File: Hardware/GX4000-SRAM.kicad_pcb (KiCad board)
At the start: 2 copper layers, 7 parts, among them U1 IS62C1024AL-35QLI, U2 74HCT573, U3 74LVC1G32, U4 TMS4464, U5 TMS4464

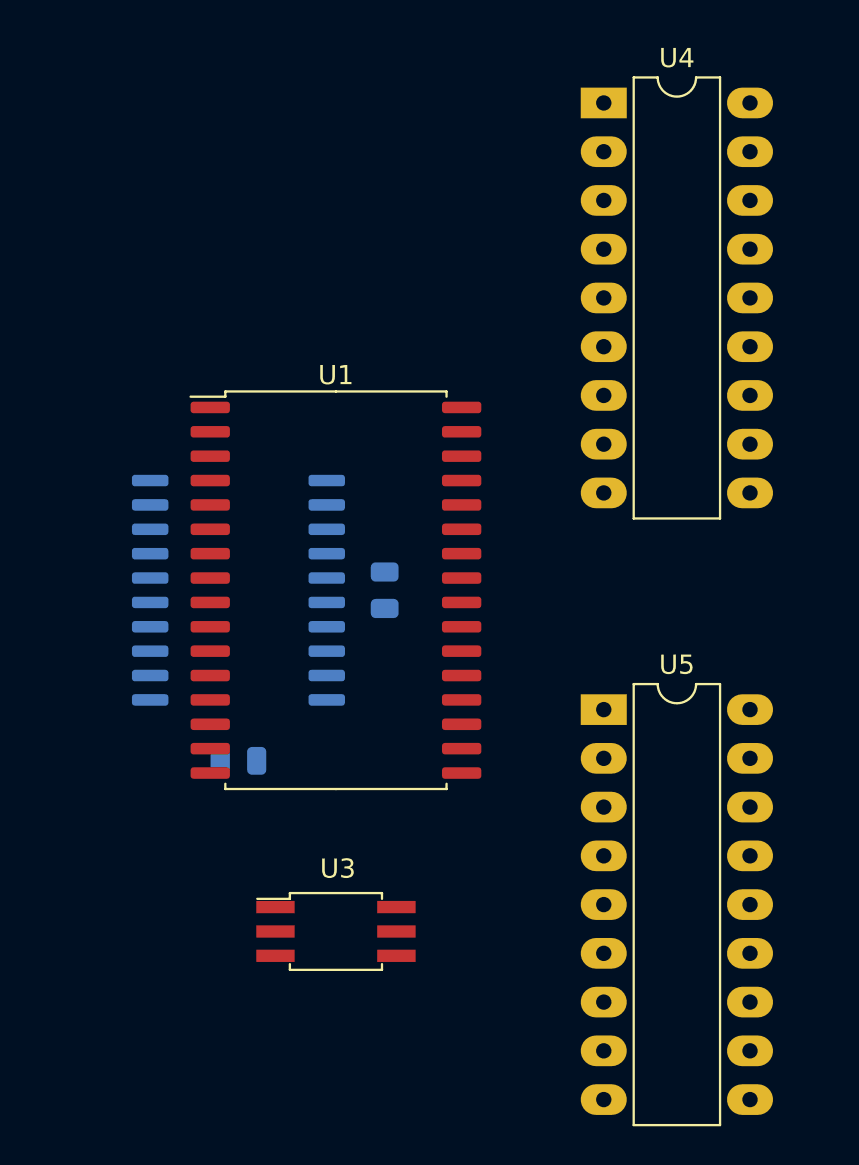
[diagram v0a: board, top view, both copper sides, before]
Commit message: Fixes the expacement between U10 and U11
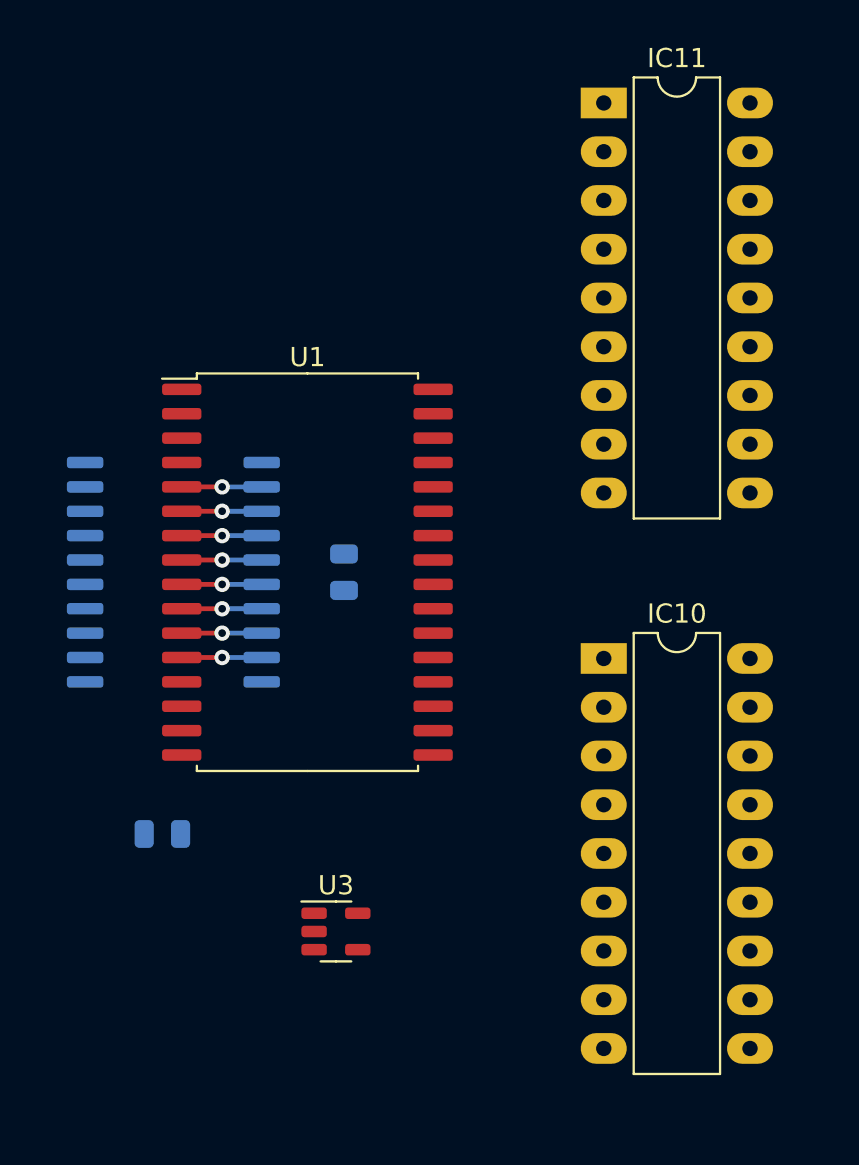
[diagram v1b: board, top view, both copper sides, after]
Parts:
- U3: footprint Package_SO:SO-6_4.4x3.6mm_P1.27mm -> Package_TO_SOT_SMD:SOT-23-5
- moved C1 5.50 mm to (128.1, 104.1)
- moved U2 3.52 mm to (128.7, 90.5)
- moved IC10 2.66 mm to (151.1, 95.0)
- moved C2 2.32 mm to (137.6, 90.5)
- moved U1 1.76 mm to (135.7, 90.5)
- renumbered U5 to IC10, U4 to IC11
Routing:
- net /A7: track 0.00 -> 4.16 mm, vias 0 -> 1
- net /A6: track 0.00 -> 4.16 mm, vias 0 -> 1
- net /A5: track 0.00 -> 4.16 mm, vias 0 -> 1
- net /A4: track 0.00 -> 4.16 mm, vias 0 -> 1
- net /A3: track 0.00 -> 4.16 mm, vias 0 -> 1
- net /A2: track 0.00 -> 4.16 mm, vias 0 -> 1
- net /A1: track 0.00 -> 4.16 mm, vias 0 -> 1
- net /A0: track 0.00 -> 4.16 mm, vias 0 -> 1

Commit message: Release PCB
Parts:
- C1: moved to F.Cu
- U3: moved to B.Cu
- moved C1 14.1 mm to (141.4, 108.9)
- moved U3 5.93 mm to (141.5, 105.1)
- moved C2 0.71 mm to (137.3, 91.1)
- moved U2 0.07 mm to (128.8, 90.5)
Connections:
- IC10 pad 10: /MA7 -> unconnected-(IC10-Pad10)
- IC10 pad 15: /D6 -> /D2
- IC10 pad 17: /D7 -> /D3
- IC10 pad 2: /D4 -> /D0
- IC10 pad 3: /D5 -> /D1
- IC10 pad 4: /~{WE} -> unconnected-(IC10-Pad4)
- IC10 pad 6: /MA6 -> unconnected-(IC10-Pad6)
- IC10 pad 8: /MA4 -> unconnected-(IC10-Pad8)
- IC11 pad 10: unconnected-(IC11-Pad10) -> /MA7
- IC11 pad 15: /D2 -> /D6
- IC11 pad 17: /D3 -> /D7
- IC11 pad 2: /D0 -> /D4
- IC11 pad 3: /D1 -> /D5
- IC11 pad 4: unconnected-(IC11-Pad4) -> /~{WE}
- IC11 pad 6: unconnected-(IC11-Pad6) -> /MA6
- IC11 pad 8: unconnected-(IC11-Pad8) -> /MA4
- U3 pad 1: /~{RAS} -> /~{CAS}
- U3 pad 2: /~{CAS} -> /~{RAS}
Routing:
- net /MA0: track 0.00 -> 67.5 mm, vias 0 -> 1
- net /MA1: track 0.00 -> 66.9 mm, vias 0 -> 1
- net /MA5: track 0.00 -> 61.8 mm, vias 0 -> 1
- net /MA3: track 0.00 -> 60.2 mm, vias 0 -> 1
- net /MA2: track 0.00 -> 56.2 mm, vias 0 -> 1
- net VCC: track 0.00 -> 47.1 mm, vias 0 -> 2
- net /D4: track 0.00 -> 44.1 mm, vias 0 -> 1
- net /MA7: track 0.00 -> 43.0 mm, vias 0 -> 1
- net /~{RAS}: track 0.00 -> 40.4 mm
- net /D7: track 0.00 -> 40.2 mm, vias 0 -> 1
- net /D6: track 0.00 -> 38.9 mm, vias 0 -> 1
- net /D5: track 0.00 -> 38.7 mm, vias 0 -> 1
- net /D2: track 0.00 -> 38.2 mm, vias 0 -> 1
- net /MA4: track 0.00 -> 38.1 mm, vias 0 -> 1
- net /MA6: track 0.00 -> 34.0 mm, vias 0 -> 1
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- added copper zone on B.Cu, net GND
- added copper zone on F.Cu, net GND
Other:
- board outline added: 40.6 x 53.3 mm
